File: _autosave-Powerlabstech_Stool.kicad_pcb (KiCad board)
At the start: 2 copper layers, 75 x 85 mm, 54 parts, among them J1 Screw_Terminal_01x02, J2 Conn_01x02_Pin, J3 Conn_01x02_Pin, J4 Conn_01x05_Socket, J5 Screw_Terminal_01x02, K1 SANYOU_SRD_Form_C, Q1 Q_NMOS_GSD, Q2 Q_NMOS_GSD, Q3 Q_NMOS_GSD, Q4 Q_NMOS_GSD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

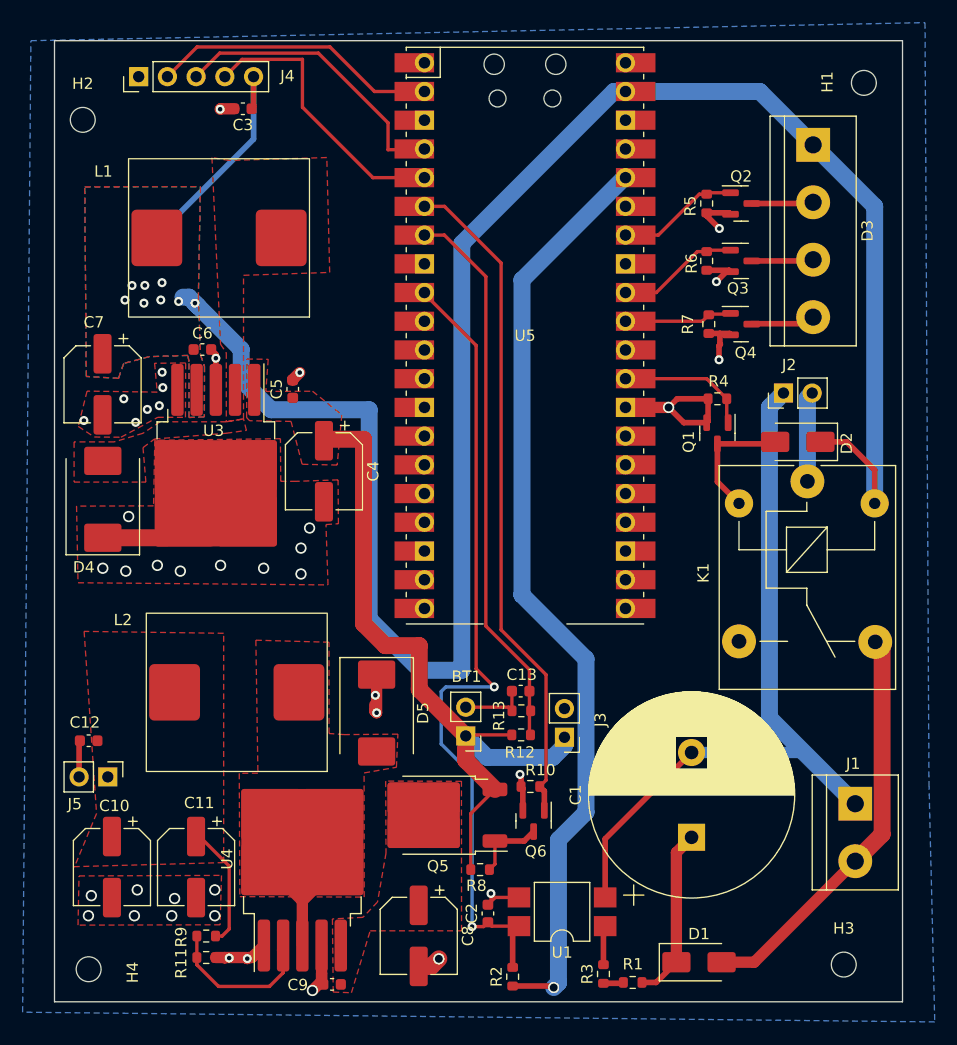
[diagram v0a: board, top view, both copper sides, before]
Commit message: Added the USB output and added the output files
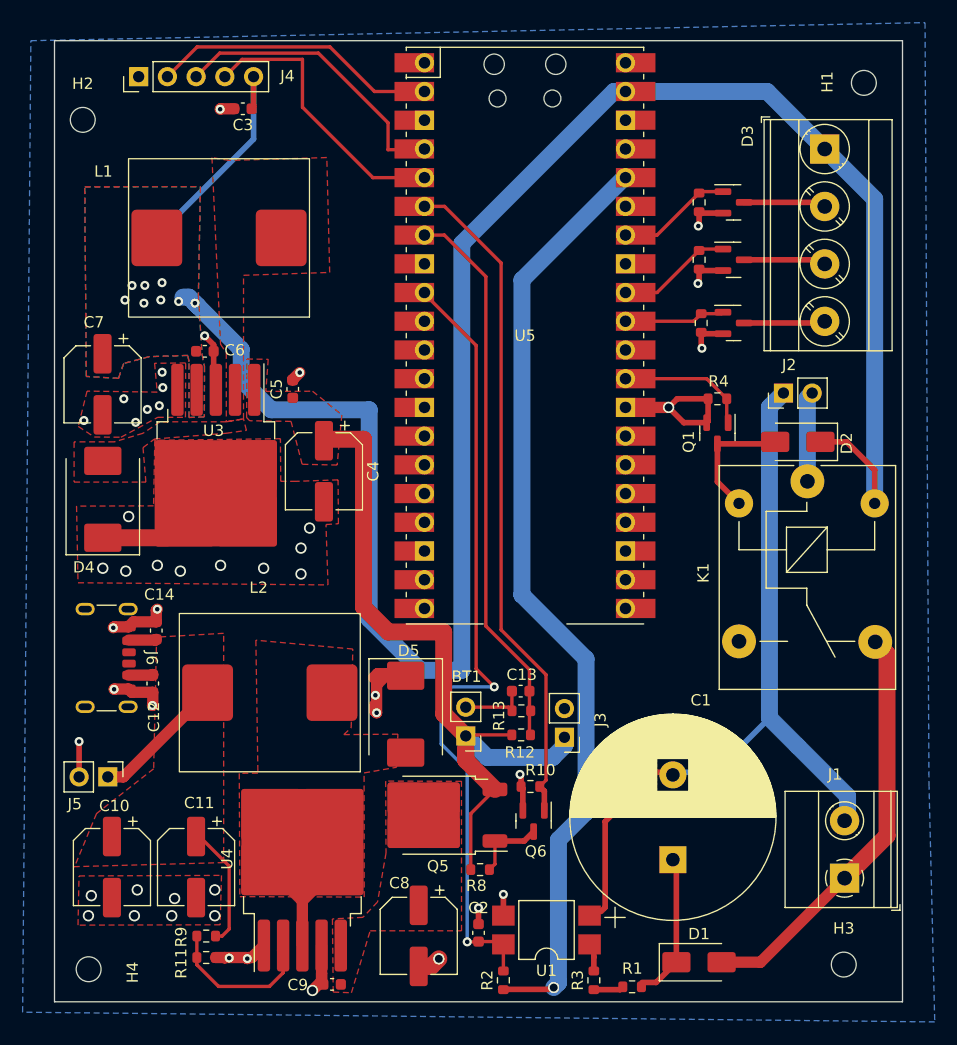
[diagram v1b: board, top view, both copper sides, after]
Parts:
- added C14: 100nF, Capacitor_SMD:C_0603_1608Metric, F.Cu at (85.5, 110.7)
- added G***: LOGO, LOGO, B.Cu at (89.5, 104.4)
- added J6: USB_C_Receptacle_PowerOnly_6P, Connector_USB:USB_C_Receptacle_GCT_USB4125-xx-x_6P_TopMnt_Horizontal, F.Cu at (80.0, 113.1)
- D3: footprint TerminalBlock:TerminalBlock_bornier-4_P5.08mm -> TerminalBlock_Phoenix:TerminalBlock_Phoenix_MKDS-3-4-5.08_1x04_P5.08mm_Horizontal
- J1: footprint TerminalBlock:TerminalBlock_bornier-2_P5.08mm -> TerminalBlock_Phoenix:TerminalBlock_Phoenix_MKDS-1,5-2-5.08_1x02_P5.08mm_Horizontal
- moved C12 7.60 mm to (85.2, 115.3), turned to -90 degrees
- moved J1 6.65 mm to (146.4, 132.6), turned to 90 degrees
- moved L2 2.92 mm to (101.0, 116.2)
- moved C1 2.58 mm to (131.2, 130.9)
- moved D5 2.57 mm to (107.6, 118.1)
- moved U1 2.12 mm to (120.0, 137.2)
- moved C2 1.90 mm to (114.0, 137.4)
- moved D3 1.09 mm to (144.6, 68.1)
- moved R3 1.02 mm to (124.2, 141.6)
- moved R2 0.88 mm to (116.2, 141.6)
- moved Q4 0.68 mm to (136.6, 83.5)
- moved R7 0.68 mm to (133.7, 83.5)
- moved Q2 0.68 mm to (136.6, 72.8)
- moved Q3 0.68 mm to (136.6, 77.9)
- moved R5 0.68 mm to (133.5, 72.8)
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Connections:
- J1 pad 1: /NEUTRAL -> /LIVE
- J1 pad 2: /LIVE -> /NEUTRAL
- U5 pad 38: GND -> unconnected-(U5-GND-Pad38)
- U5 pad 8: GND -> unconnected-(U5-GND-Pad8)
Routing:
- net /sw_OUT: track 11.1 -> 27.6 mm
- net GND: track 74.1 -> 84.3 mm, vias 40 -> 46
- net /LED_RED_OUT: track 5.48 -> 7.27 mm
- net /LED_GREEN_OUT: track 5.48 -> 7.27 mm
- net /LED_BLUE_OUT: track 5.67 -> 7.18 mm
- net /MAINS_SENSE: track 72.6 -> 71.1 mm
- net /main_det_ret: track 15.4 -> 13.9 mm
- net /NEUTRAL: track 65.9 -> 67.4 mm
- net Net-(R3-Pad2): track 3.47 -> 2.25 mm
- net /BATT_POS: track 66.0 -> 67.1 mm
- net +3.3V: track 82.4 -> 83.4 mm
- net Net-(R1-Pad2): track 1.79 -> 2.66 mm
- net /LED_BLUE: track 9.70 -> 8.95 mm
- net /LED_GREEN: track 11.0 -> 10.2 mm
- net /LED_RED: track 11.0 -> 10.3 mm
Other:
- board text added: "HIGH VOLTAGE"
